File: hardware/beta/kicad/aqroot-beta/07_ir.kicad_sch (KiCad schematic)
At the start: 0 parts

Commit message: AQROOT Beta: capture I2C, audio, IR, and SPI-A subsystems
Reconciles the active KiCad project from OneDrive into the canonical
repository. The four subsystem sheets existed here only as 169-byte
empty stubs; the real schematic capture had been done in the OneDrive
working copy.

Sheets brought in:
  03_spi_a_display_sd.kicad_sch   stub ->  62136 bytes
  05_i2c_devices.kicad_sch        stub ->  59631 bytes
  06_audio.kicad_sch              stub ->  55263 bytes
  07_ir.kicad_sch                 stub ->  50216 bytes

Also updated: aqroot-Beta.kicad_sch (root sheet, now carrying the
child sheet instances) and aqroot-Beta.kicad_pro.

03_spi_a_display_sd instantiates AQROOT_Beta:ILI9341_FT6236_MODULE_-
PLACEHOLDER; its cached symbol matches libraries/AQROOT_Beta.kicad_sym
exactly (13 pins, blank footprint, on_board=no).

Deliberately not taken from OneDrive:
  - sym-lib-table / fp-lib-table. The OneDrive copies hard-code an
    absolute P:/ path to this repository's library; the versions kept
    here use ${KIPRJMOD} and stay portable.
  - aqroot-Beta.kicad_prl (local project state) and .history/
    (2388 editor-history files, 5.87 MB).

Sheets identical on both sides and therefore untouched: 01_power_tree,
02_mcu_core, 04_spi_b_radios_nfc, 08_buttons_expanders,
09_community_header, aqroot-Beta.kicad_pcb.

Every copied file was verified by SHA-256 against its source, and each
staged blob is byte-identical to the working-tree file: CRLF endings
are preserved per .gitattributes, with no EOL normalization or
reformatting.

Co-Authored-By: Claude Opus 5 <noreply@anthropic.com>
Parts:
- added C11: 4.7uF, symbol Device:C
- added C12: TBD, symbol Device:C
- added D1: TSAL6200, LED_THT:LED_D5.0mm, symbol Device:LED
- added Q1: NMOS_TBD, symbol Transistor_FET:Q_NMOS_GSD
- added R21, R22: 100R, symbol Device:R
- added R23: 100K, symbol Device:R
- added R24: TBD, symbol Device:R
- added U6: TSOP38238, AQROOT_Beta:Vishay_TSOP382xx_Minicast_3Pin_P2.54mm, symbol AQROOT_Beta:TSOP38238
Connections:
- new net +3V3: R21.1
- new net GND: C11.2, C12.1, Q1.2 (S), R23.2, U6.2 (GND)
- new net IR_GATE: Q1.1 (G), R22.2, R23.1
- new net IR_LED_A: D1.2 (A), R24.1
- new net IR_LED_K: D1.1 (K), Q1.3 (D)
- new net IR_LED_SUPPLY_TBD: C12.2, R24.2
- new net IR_RX_GPIO44: U6.1 (OUT)
- new net IR_RX_VS_LOCAL: C11.1, R21.2, U6.3 (VS)
- new net IR_TX_GPIO16: R22.1
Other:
- note added: "IR RECEIVER PLACEMENT KEEP TSOP38238 PHYSICALLY SEPARATED FROM TSAL6200 KEEP RECEIVER OUTSIDE THE LED DIRECT EMISSION CONE KEEP TX CURRENT LOOP AWAY FROM RECEIVER SUPPLY/RETURN"
- note added: "IR TRANSMITTER - PARTS PENDING Q1 LOGIC-LEVEL NMOS NOT SELECTED R22 = 100R GATE SERIES R23 = 100k GATE PULL-DOWN R24 CURRENT-LIMIT VALUE PENDING IR_LED_SUPPLY RAIL PENDING LOCAL BULK CAPACITOR VALUE PENDING DO NOT CONNECT TSAL6200 DIRECTLY TO A POWER RAIL DO NOT ROUTE UNTIL PULSE CURRENT IS SELECTED"

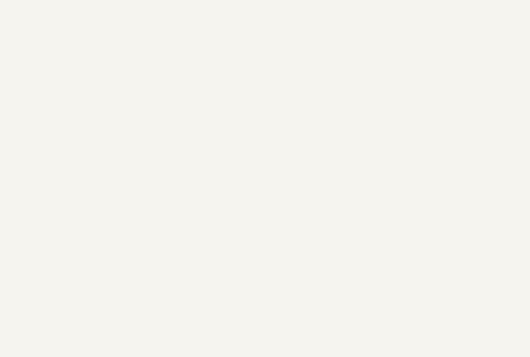
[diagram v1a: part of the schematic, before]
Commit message: AQROOT Beta: add ERC power flags
Five nets are driven from outside the schematic or through passive/bidi
paths, so ERC could not find a power source and raised
power_pin_not_driven. Each now carries a stock power:PWR_FLAG.

  #FLG0101  USB_VBUS_CHG      01_power_tree   (drives U11.10 IN)
  #FLG0102  BAT_PROTECTED_P   01_power_tree   (drives U14.2 CELL)
  #FLG0103  IR_RX_VS_LOCAL    07_ir           (drives U6.3 VS)
  #FLG0104  ACC_3V3_SW        09_community    (drives U16.8 VCCB)
  #FLG0105  GND               09_community    (drives D2.2 GND)

PWR_FLAG did not previously exist in this project, so the stock
power:PWR_FLAG definition is added to the lib_symbols cache of the three
sheets that use it, appended after power:GND to keep the alphabetical order
KiCad writes.

Each flag is a self-contained cluster in verified-empty space: PWR_FLAG ->
5.08 mm wire -> a local label carrying the net name (or, for GND, a new
power:GND symbol #PWR0178, since GND is global and carries no labels).
Nothing existing was moved or rewired - the diff is insertions only, 0
deletions in all three files.

All coordinates are on the 1.27 mm grid (a first attempt off-grid raised 11
endpoint_off_grid violations and was reverted rather than committed).

Verified with kicad-cli: all sheets still parse and plot; netlist
pin-to-net mapping is unchanged for every pre-existing pin - no topology
change. BAT_CONNECTOR_P {J4.1} and BAT_PROTECTED_P {C25.1, C36.1, U11.2,
U14.2, U14.3} remain distinct; the parked reverse-polarity placeholder is
untouched. The 20 intentional exclusions and all 46 ERC rule severities are
unchanged. Real ERC 13 -> 10.

Known trade: two new pin_to_pin WARNINGS appear where a flag shares a net
with a bidirectional pin - U11.2 BAT on BAT_PROTECTED_P and U4.1 SDO on
GND. That is inherent to PWR_FLAG's power_out pin type and is the same
warning class as the existing BMI270 ASDx/ASCx items. Five errors traded
for two warnings; left for the same judgement call.

Co-Authored-By: Clau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
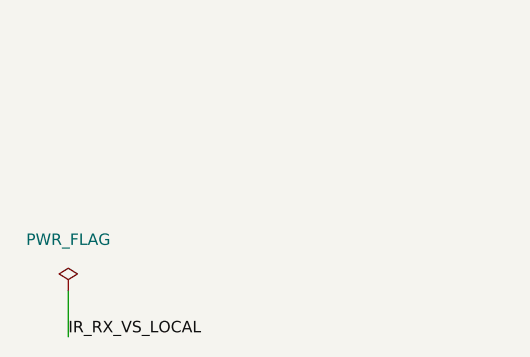
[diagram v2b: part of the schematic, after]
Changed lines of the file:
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@@
+	(wire
+		(pts
+			(xy 20.32 185.42) (xy 20.32 190.5)
+		)
+		(stroke
+			(width 0)
+			(type default)
+		)
+	)
 	(wire
 		(pts
@@
 			(width 0)
 			(type default)
+		)
+	)
+	(label "IR_RX_VS_LOCAL"
+		(at 20.32 190.5 0)
+		(effects
+			(font
+				(size 1.27 1.27)
+			)
+			(justify left bottom)
 		)
 	)
@@
 		)
 	)
+	(symbol
+		(lib_id "power:PWR_FLAG")
+		(at 20.32 185.42 0)
+		(unit 1)
+		(body_style 1)
+		(exclude_from_sim no)
+		(in_bom yes)
+		(on_board yes)
+		(in_pos_files yes)
+		(dnp no)
+		(property "Reference" "#FLG0103"
+			(at 20.32 181.61 0)
+			(hide yes)
+			(show_name no)
+			(do_not_autoplace no)
+			(effects
+				(font
+					(size 1.27 1.27)
+				)
+			)
+		)
+		(property "Value" "PWR_FLAG"
+			(at 20.32 179.705 0)
+			(show_name no)
+			(do_not_autoplace no)
+			(effects
+				(font
+					(size 1.27 1.27)
+				)
+			)
+		)
+		(property "Footprint" ""
+			(at 20.32 185.42 0)
+			(hide yes)
+			(show_name no)
+			(do_not_autoplace no)
+			(effects
+				(font
+					(size 1.27 1.27)
+				)
+			)
+		)
+		(property "Datasheet" ""
+			(at 20.32 185.42 0)
+			(hide yes)
+			(show_name no)
+			(do_not_autoplace no)
+			(effects
+				(font
+					(size 1.27 1.27)
+				)
+			)
+		)
+		(property "Description" "Special symbol for telling ERC where power comes from"
+			(at 20.32 185.42 0)
+			(hide yes)
+			(show_name no)
+			(do_not_autoplace no)
+			(effects
+				(font
+					(size 1.27 1.27)
+				)
+			)
+		)
+		(pin "1"
+		)
+		(instances
+			(project "aqroot-Beta"
+				(path "/8a0ad1ee-a49e-4cff-9a78-44823e373405/d14ac91a-547d-41d4-b6d8-03779253a1ea"
+					(reference "#FLG0103")
+					(unit 1)
+				)
+			)
+		)
+	)

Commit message: AQROOT Beta: assign standard passive footprints
Assigns footprints to 40 passives whose package is unambiguous from
existing project precedent. Property-value edits only - no symbol, wire,
label or net touched.

  28 resistors -> Resistor_SMD:R_0603_1608Metric
     R1 R2 R3-R17 R18 R19 R20 R21 R22 R23 R25 R26 R27 R28 R29
     Basis: all 39 already-assigned resistors in the project are 0603, and
     every one of these is signal-level (pull-ups, dividers, series
     termination, MOSFET gate network).

  12 capacitors -> Capacitor_SMD:C_0603_1608Metric
     C1 C2 C4 C5 C6 C7 C8 C9 C13 C14 C16 C17
     Basis: 100nF is 5/5 and 1uF is 4/4 for 0603 among already-assigned
     capacitors - unanimous.

DELIBERATELY NOT ASSIGNED - split precedent, needs a decision:
  C3, C15, C10  10uF   -> project uses BOTH C_1206 (x2) and C_0805 (x1)
  C11           4.7uF  -> single 0805 precedent, different subsystem
Bulk capacitors must not be blindly converted to 0603, and the existing
precedent does not settle 0805 vs 1206.

Also untouched per instruction: C12/R24/Q1 (TBD), C18/C19 (placeholder),
L1/L2, mechanical switches and connectors, and the four RF/module
placeholders.

Separately noted, NOT changed here: C24 is 22uF 25V X7R with
C_0603_1608Metric already assigned. A 22uF 25V X7R does not exist in 0603
and the project's other 22uF parts use 1206/0805 - this looks like a
pre-existing error and is flagged for the BOM pass, not silently altered.

Verified with kicad-cli: netlist pin-to-net mapping byte-identical before
and after. ERC unchanged: raw 48, unique 24, excluded 24, real 0.
Footprint coverage 97 -> 137 of 166 components.

Co-Authored-By: Claude Opus 5 <noreply@anthropic.com>
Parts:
- R21, R22, R23: footprint (none) -> Resistor_SMD:R_0603_1608Metric
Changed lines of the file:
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@@
 			)
 		)
-		(property "Footprint" ""
+		(property "Footprint" "Resistor_SMD:R_0603_1608Metric"
 			(at 175.26 37.338 90)
 			(hide yes)
@@
 			)
 		)
-		(property "Footprint" ""
+		(property "Footprint" "Resistor_SMD:R_0603_1608Metric"
 			(at 172.212 58.42 90)
 			(hide yes)
@@
 			)
 		)
-		(property "Footprint" ""
+		(property "Footprint" "Resistor_SMD:R_0603_1608Metric"
 			(at 136.652 60.96 90)
 			(hide yes)

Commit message: AQROOT Beta: assign remaining generic bulk-cap footprints
Assigns Capacitor_SMD:C_0805_2012Metric to the four bulk capacitors left
open by the standard-passive pass.

  C3   10uF   +3V3                  02_mcu_core     generic bulk decoupling
  C15  10uF   +3V3                  03_spi_a        generic bulk decoupling
  C10  10uF   +3V3                  06_audio        generic bulk decoupling
  C11  4.7uF  /07_IR/IR_RX_VS_LOCAL 07_ir           TSOP382 supply RC

Basis: these are NOT regulator input/output capacitors. The project's 1206
precedent (C26/C27 CIN, C29-C32 COUT) is a TPS63020-specific requirement -
the kicad README states '1206 preferred ... Close to VIN/PGND' for those
parts only, so it does not generalise. For generic 10uF/10V and 4.7uF/10V
bulk on a 3.3V rail, 0805 is adequate and is the project's generic
precedent (C33, C20). C11's role is documented at libraries/README.md:1264
as Vishay's TSOP382 application R1/C1 supply filter, paired with R21 100R.

Property-value edits only - four lines. No value, symbol, wire, label or
net touched.

Verified with kicad-cli: netlist pin-to-net mapping byte-identical before
and after. ERC unchanged: raw 48, unique 24, excluded 24, real 0.

Still open and deliberately untouched: exact MPNs and DC-bias derating for
these parts. A 10uF/10V 0805 X7R typically retains only ~60-70% of its
nominal capacitance at 3.3V, so effective capacitance must be confirmed at
the BOM pass - the package is locked here, the part is not.

Co-Authored-By: Claude Opus 5 <noreply@anthropic.com>
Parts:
- C11: footprint (none) -> Capacitor_SMD:C_0805_2012Metric
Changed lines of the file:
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@@
 			)
 		)
-		(property "Footprint" ""
+		(property "Footprint" "Capacitor_SMD:C_0805_2012Metric"
 			(at 155.9052 74.93 0)
 			(hide yes)

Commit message: AQROOT Beta: lock resolved power and IR component metadata
Records exact MPN / manufacturer / package metadata for four parts whose
selection is now locked. Footprints deliberately left BLANK - locking a part
and verifying its land pattern are separate gates.

  L1   XFL4020-152MEC   Coilcraft                     1.5uH (was '1.5uH XFL4020-152MEC')
  L2   74438357010      Wurth Elektronik              1uH   (was '1uH SHIELDED')
  Q1   AO3400A          Alpha & Omega Semiconductor   AO3400A (was 'NMOS_TBD')
  U16  TCA9517ADGKR     Texas Instruments             TCA9517ADGK (value unchanged)

Instance-level properties only, on stock symbols (Device:L,
Transistor_FET:Q_NMOS_GSD, Logic_LevelTranslator:TCA9517ADGK) - no stock
library was edited and no project-local symbol was touched.

Deliberately NOT recorded, per the no-fabrication rule: Isat, DCR, current
ratings, body dimensions, Vds/Id/Rds(on). Each Note says to take those from
the manufacturer datasheet at BOM lock rather than from memory.

Q1 pin mapping cross-checked against the existing wiring: Q_NMOS_GSD gives
1 Gate / 2 Source / 3 Drain, and the schematic already has 1 -> IR_GATE,
2 -> GND, 3 -> IR_LED_K. Consistent, but the Note flags that AO3400A's real
pin order must be confirmed against the AOS datasheet before a footprint is
assigned. Topology and GPIO mapping unchanged.

L2's Note additionally records that its current rating still has to be
checked against the TI TPS61023 5V design calculation.

U12, U14 and U15 were inspected and already carried complete and correct
metadata - no change was needed. U12's apparent 16-pin/14-pin conflict is
explained by its own Note: pins 15 and 16 are KiCad-only logical numbers for
the unnumbered PGND pad and the exposed thermal pad, so it is a genuine
14-pin DSJ.

Verified with kicad-cli: netlist pin-to-net mapping byte-identical, ERC
unchanged raw 48 / unique 24 / excluded 24 / real 0.

Co-Authored-By: Claude Opus 5 <noreply@anthropic.com>
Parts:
- Q1: value NMOS_TBD -> AO3400A; MPN (none) -> AO3400A; Manufacturer (none) -> Alpha & Omega Semiconductor; Note (none) -> IR LED low-side driver. Symbol Transistor_FET:Q_NMOS_GSD ma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; Package (none) -> SOT-23-3 - LOCKED. Footprint BLOCKED: needs the official AO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
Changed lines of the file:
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@@
 			)
 		)
-		(property "Value" "NMOS_TBD"
+		(property "Value" "AO3400A"
 			(at 203.2 48.2599 0)
 			(show_name no)
@@
 			(at 196.85 46.99 0)
 			(hide yes)
+			(show_name no)
+			(do_not_autoplace no)
+			(effects
+				(font
+					(size 1.27 1.27)
+				)
+			)
+		)
+		(property "Note" "IR LED low-side driver. Symbol Transistor_FET:Q_NMOS_GSD maps pin 1 Gate / 2 Source / 3 Drain, matching the existing wiring (1 -> IR_GATE, 2 -> GND, 3 -> IR_LED_K). VERIFY that AO3400A pin order is G/S/D against the AOS datasheet before assigning a footprint. Vds/Id/Rds(on) NOT recorded here."
+			(at 196.85 46.99 0)
+			(hide yes)
+			(show_name no)
+			(do_not_autoplace no)
+			(effects
+				(font
+					(size 1.27 1.27)
+				)
+			)
+		)
+		(property "Package" "SOT-23-3 - LOCKED. Footprint BLOCKED: needs the official AOS recommended land pattern."
+			(at 196.85 46.99 0)
+			(hide yes)
+			(show_name no)
+			(do_not_autoplace no)
+			(effects
+				(font
+					(size 1.27 1.27)
+				)
+			)
+		)
+		(property "Manufacturer" "Alpha & Omega Semiconductor"
+			(at 196.85 46.99 0)
+			(hide yes)
+			(show_name no)
+			(do_not_autoplace no)
+			(effects
+				(font
+					(size 1.27 1.27)
+				)
+			)
+		)
+		(property "MPN" "AO3400A"
+			(at 196.85 46.99 0)
+			(hide yes)

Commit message: Footprints: verify AO3400A SOT-23; record third-pass results
Q1 AO3400A assigned Package_TO_SOT_SMD:SOT-23 as VERIFIED_IPC_ALTERNATE.

AOS publishes package geometry separately from the device datasheet - at
res/package/SOT23.pdf, doc PO-00001 rev N - which is why the earlier pass
found nothing. Retrieved and rasterized:

  AOS recommended land : pads 0.80 x 0.80, row-to-row 2.40, pitch 0.95
  AOS package          : e 0.95 BSC, e1 1.90 BSC, D 2.90, E 2.80, E1 1.60,
                         b 0.40 (all nominal)
  KiCad SOT-23         : 3 pads, pitch 0.95 EXACT, same 2+1 lead arrangement,
                         pads 1.475 x 0.6 at +/-0.9375

Copper proportions differ - AOS shorter/wider, KiCad longer/narrower - but
both straddle the 2.80 mm lead span, and this is an ordinary leaded package,
so Class A applies and vendor-exact copper is not required.

Pin order is now CONFIRMED rather than assumed: the datasheet package view
and symbol both show G and S on the two-lead side and D on the single-lead
side, giving 1 G / 2 S / 3 D. That matches Q_NMOS_GSD and the existing
wiring (1 -> IR_GATE, 2 -> GND, 3 -> IR_LED_K), closing the caveat recorded
when Q1's MPN was locked.

Also records the method advance that unblocked L1/L2 in the preceding commit:
vendor pages are now rasterized and the dimension leader lines read visually.
That proved the earlier text-order reasoning wrong - for Coilcraft neither
arithmetic candidate was right, because 2.37 is centre-to-centre, not a span.
Rasterization should be the default for any land pattern given as bare
numbers.

Still blocked, with attempts recorded: U12 (TI DSJ drawing absent from the
34-page datasheet), U14 (90-0065), SW9 (C&K 403), U10 (ST timed out 4x),
U5 (ADI connection reset).

Verified with kicad-cli: netlist pin-to-net mapping byte-identical, ERC
raw 48 / unique 24 / excluded 24 / real 0.

Co-Authored-By: Claude Opus 5 <noreply@anthropic.com>
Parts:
- Q1: footprint (none) -> Package_TO_SOT_SMD:SOT-23
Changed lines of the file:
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@@
 			)
 		)
-		(property "Footprint" ""
+		(property "Footprint" "Package_TO_SOT_SMD:SOT-23"
 			(at 201.93 44.45 0)
 			(hide yes)

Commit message: AQROOT Beta: finalize Beta IR driver values
Closes the parked IR supply rail and locks the two remaining IR passives.

IR_LED_SUPPLY_TBD -> +3V3. Both IR_LED_SUPPLY_TBD labels were replaced with
power:+3V3 symbols (#PWR0505, #PWR0506) placed on the same wire endpoints, so
the branch now joins the global +3V3 net rather than a sheet-local parked net.
The label was never referenced by an ERC exclusion, so no exclusion record was
touched.

R24 = 18R, 1 percent, 0805. Rail 3.3 V, TSAL6200 Vf ~1.35 V typ / ~1.6 V high,
AO3400A drop negligible at this current, so I = (3.3 - Vf) / 18R gives ~108 mA
at Vf 1.35 V and ~94 mA at Vf 1.6 V against the ~100 mA target. Peak I^2*R in
R24 is ~0.21 W at 108 mA; the 38 kHz carrier is pulsed at low duty so average
power is far below that, and 0805 is chosen for pulse-energy headroom rather
than average power. IR current is deliberately not raised - longer-range IR
tuning stays deferred post-Kickstarter.

C12 = 4.7uF, 10 V, X7R, 0805. Local IR pulse reservoir on the +3V3 IR branch so
the burst does not modulate the shared rail.

Both parts are captured as STANDARD_EIA_PASSIVE with BOM class and approved
alternates rather than a premium single MPN; DC-bias derating on C12 is flagged
for BOM-lock validation.

TOPOLOGY NOTE - the captured circuit places R24 on the high side, between +3V3
and the TSAL6200 anode, not between the LED cathode and the AO3400A drain as
the ratified brief describes. The series loop is otherwise identical
(+3V3 -> R24 -> D1 anode -> D1 cathode -> Q1 drain -> Q1 source -> GND), so the
LED current, the resistor dissipation and the gate drive are unchanged. Per the
brief's instruction not to silently rewire, the existing arrangement was left
as captured and is reported instead.

Netlist delta is exactly the intended one: C12 pin 2 and R24 pin 2 move from
/07_IR/IR_LED_SUPPLY_TBD to +3V3, that net disappears, and nothing else in the
design changes. Canonical ERC holds at 58 raw / 5 errors / 53 warnings with 58
live ex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
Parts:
- C12: value TBD -> 4.7uF; footprint (none) -> Capacitor_SMD:C_0805_2012Metric; BOM_Class (none) -> STANDARD_EIA_PASSIVE - multi-source, approved alternates, n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; Dielectric (none) -> X7R; Note (none) -> Local IR pulse reservoir on the +3V3 IR LED branch; supplie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; Package (none) -> 0805 (2012 metric); Voltage (none) -> 10V
- R24: value TBD -> 18R; footprint (none) -> Resistor_SMD:R_0805_2012Metric; BOM_Class (none) -> STANDARD_EIA_PASSIVE - multi-source, approved alternates, n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; Note (none) -> IR LED current limit on the +3V3 IR branch. Rail 3.3 V, TSA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; Package (none) -> 0805 (2012 metric); Tolerance (none) -> 1%
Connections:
- net IR_LED_SUPPLY_TBD is gone; now on net +3V3: C12.2, R24.2
